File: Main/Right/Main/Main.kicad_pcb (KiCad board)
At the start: 2 copper layers, 141.7 x 97.8 mm, 44 parts, among them SW1 RotaryEncoder_Switch_MP, SW2 Switch, U1 Arduino_Pro_Micro, U2 TRRS

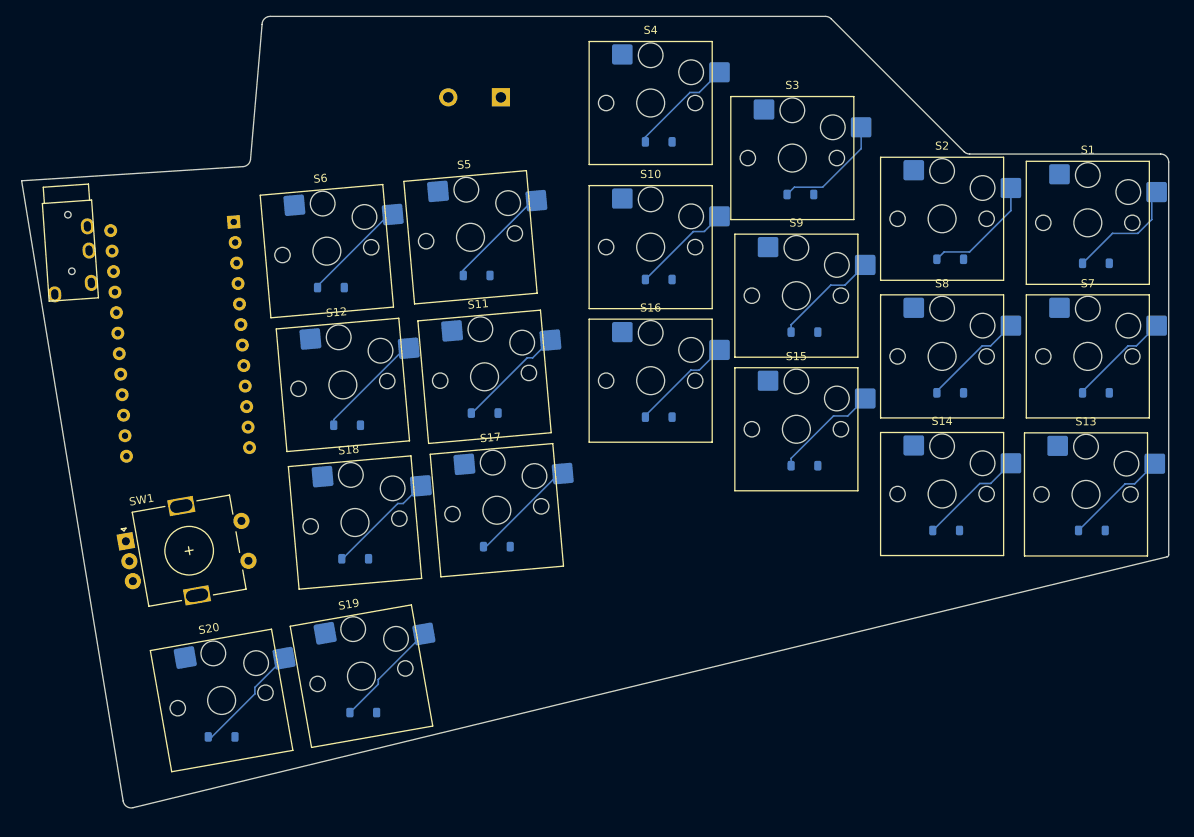
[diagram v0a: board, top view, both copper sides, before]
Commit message: changed from I2C communication between the halves to serial because it's easier with QMK
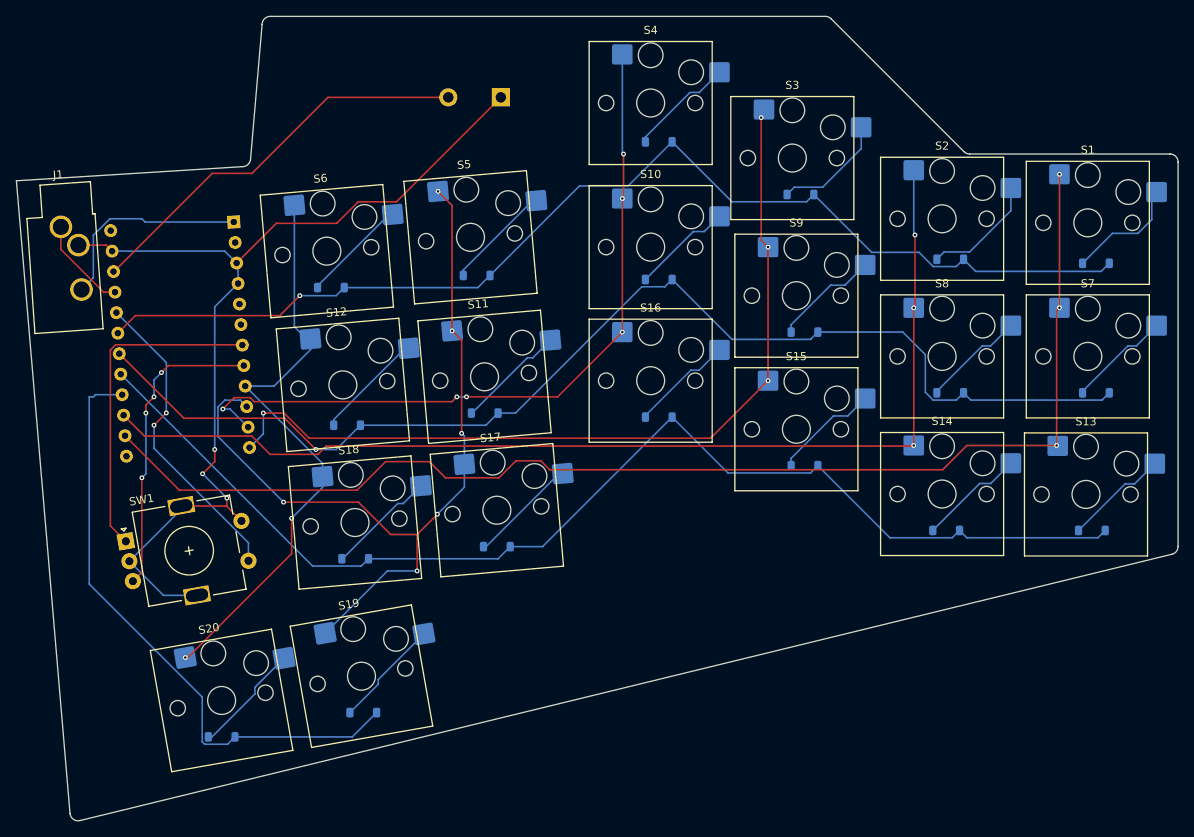
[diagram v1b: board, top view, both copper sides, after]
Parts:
- removed U2: TRRS, ScottoKeebs_Components:TRRS_PJ-320A
- added J1: AudioJack3, Connector_Audio:Jack_3.5mm_CUI_SJ1-3533NG_Horizontal_CircularHoles, F.Cu at (99.0, 76.5)
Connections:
- U1 pad 1: unconnected-(U1-TX0/PD3-Pad1) -> Serial
- U1 pad 5: SDA -> unconnected-(U1-2/PD1-Pad5)
- U1 pad 6: SCL -> unconnected-(U1-3/PD0-Pad6)
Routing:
- net 0 Column: track 0.00 -> 156.5 mm, vias 0 -> 3
- net 2 Row: track 0.00 -> 147.1 mm
- net 1 Row: track 0.00 -> 146.7 mm, vias 0 -> 1
- net 0 Row: track 0.00 -> 140.8 mm, vias 0 -> 1
- net 1 Column: track 0.00 -> 134.2 mm, vias 0 -> 3
- net GND: track 0.00 -> 122.5 mm, vias 0 -> 3
- net 2 Column: track 0.00 -> 105.5 mm, vias 0 -> 4
- net 4 Column: track 0.00 -> 102.7 mm, vias 0 -> 6
- net 3 Column: track 0.00 -> 92.2 mm, vias 0 -> 6
- net 3 Row: track 0.00 -> 75.8 mm
- net 5 Column: track 0.00 -> 73.4 mm, vias 0 -> 2
- net RST: track 0.00 -> 50.3 mm
- net Net-(U1-4/PD4): track 0.00 -> 41.0 mm
- net Net-(U1-A3/PF4): track 0.00 -> 38.7 mm, vias 0 -> 2
- net Net-(U1-5/PC6): track 0.00 -> 37.8 mm, vias 0 -> 4
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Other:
- board size 141.7 x 97.8 mm -> 143.5 x 99.4 mm
